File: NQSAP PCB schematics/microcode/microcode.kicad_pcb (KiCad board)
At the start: 2 copper layers, 102 x 96 mm, 58 parts, among them J1 Bus, J2 Bus, J5 Conn_02x08, J6 Conn_02x08, U1 28C256, U2 28C256, U3 28C256

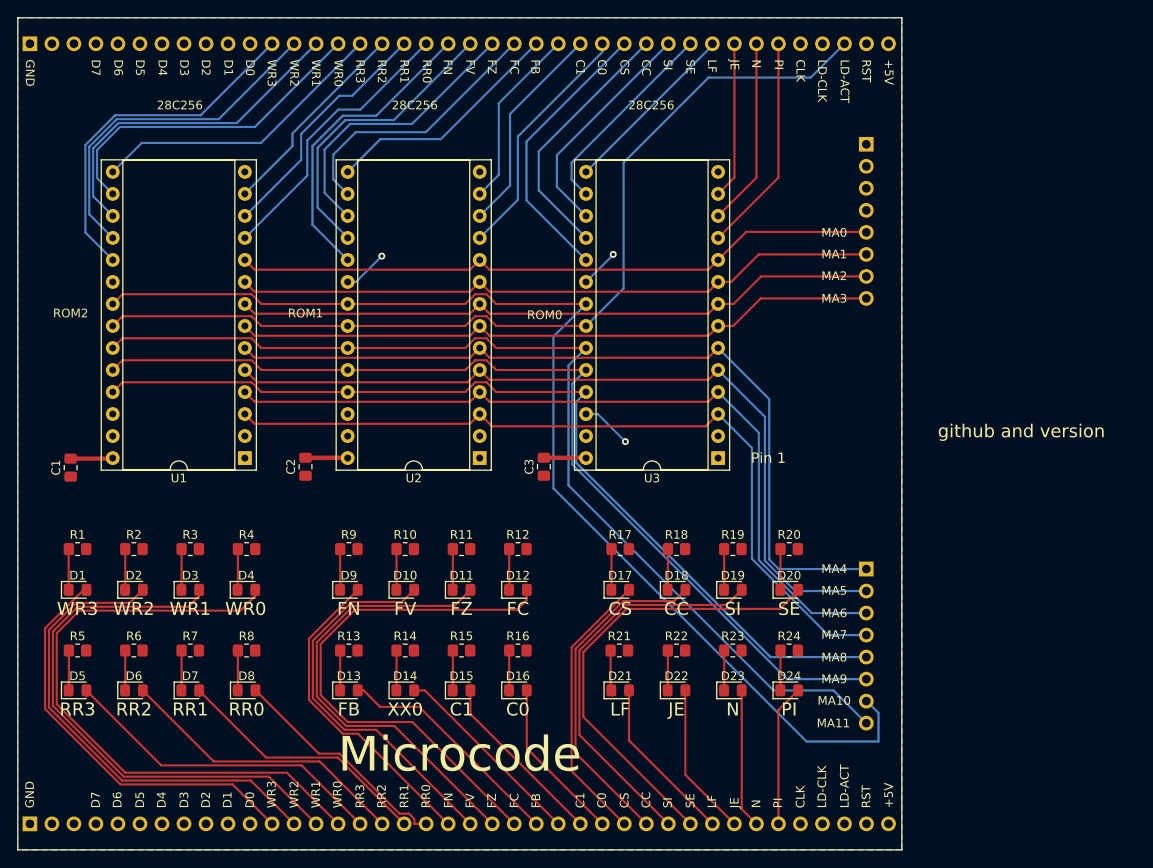
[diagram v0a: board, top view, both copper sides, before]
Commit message: Add Microcode and IR/RC modules.  Add clock circuit to Loader module.
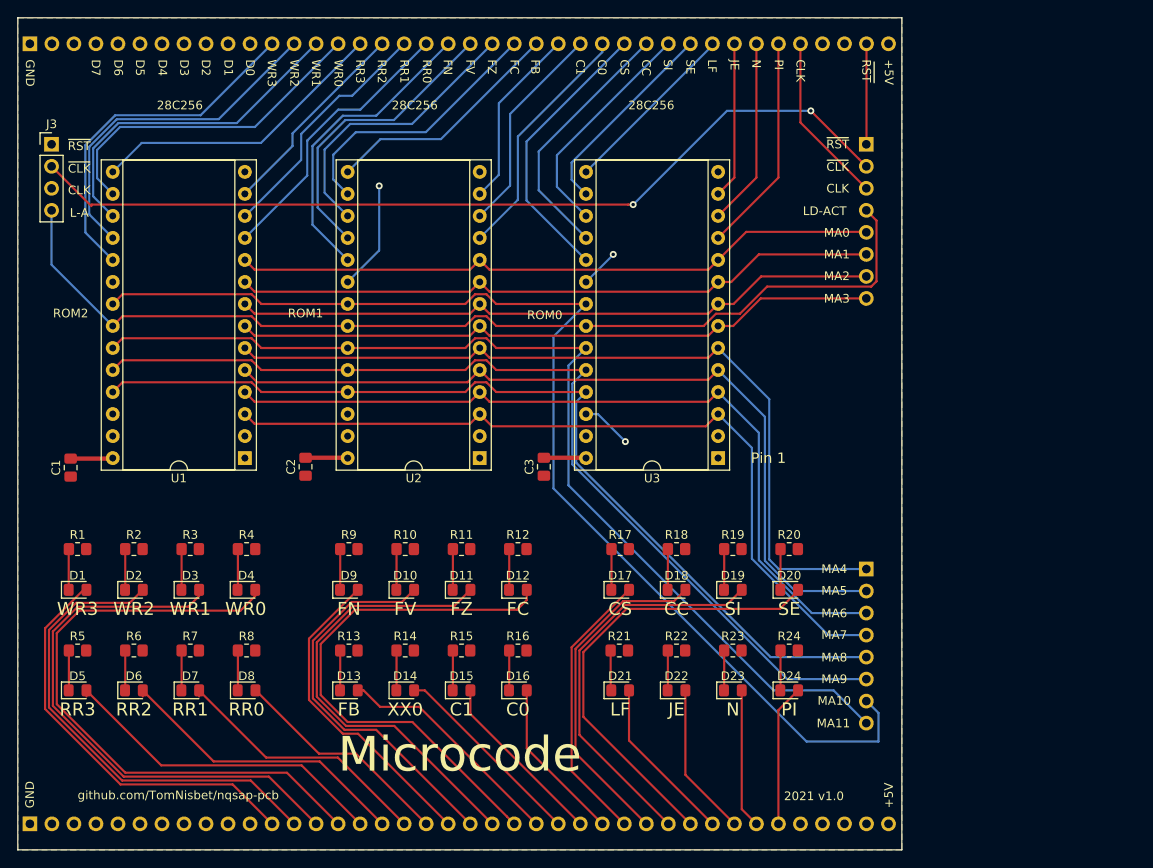
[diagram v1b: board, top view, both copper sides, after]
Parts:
- added J3: IC-LT, Connector_PinHeader_2.54mm:PinHeader_1x04_P2.54mm_Vertical, F.Cu at (88.9, 57.6)
- J5: value Conn_02x08 -> IC-RT
- J6: value Conn_02x08 -> IC-RB
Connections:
- J1 pad 36: Net-(J1-Pad36) -> CLK
- J1 pad 38: LD-ACT -> Net-(J1-Pad38)
- J1 pad 39: Net-(J1-Pad39) -> ~RST
- J5 pad 1: Net-(J5-Pad1) -> ~RST
- J5 pad 2: Net-(J5-Pad2) -> ~CLK
- J5 pad 3: Net-(J5-Pad3) -> CLK
- J5 pad 4: Net-(J5-Pad4) -> LD-ACT
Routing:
- net ~CLK: track 0.00 -> 103.3 mm, vias 0 -> 2
- net CLK: track 0.00 -> 19.8 mm
- net ~RST: track 0.00 -> 11.6 mm
- net LD-ACT: track 108.3 -> 117.0 mm
- net GND: track 15.5 -> 22.9 mm
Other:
- board text added: "2021 v1.0"
- board text added: "L-A"
- board text added: "github.com/TomNisbet/nqsap-pcb"
- board text added: "~CLK"
- board text added: "~RST"
- board text removed: "LD-CLK"
- board text removed: "github and version"

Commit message: Add RAM, update and add gerbers for new boards
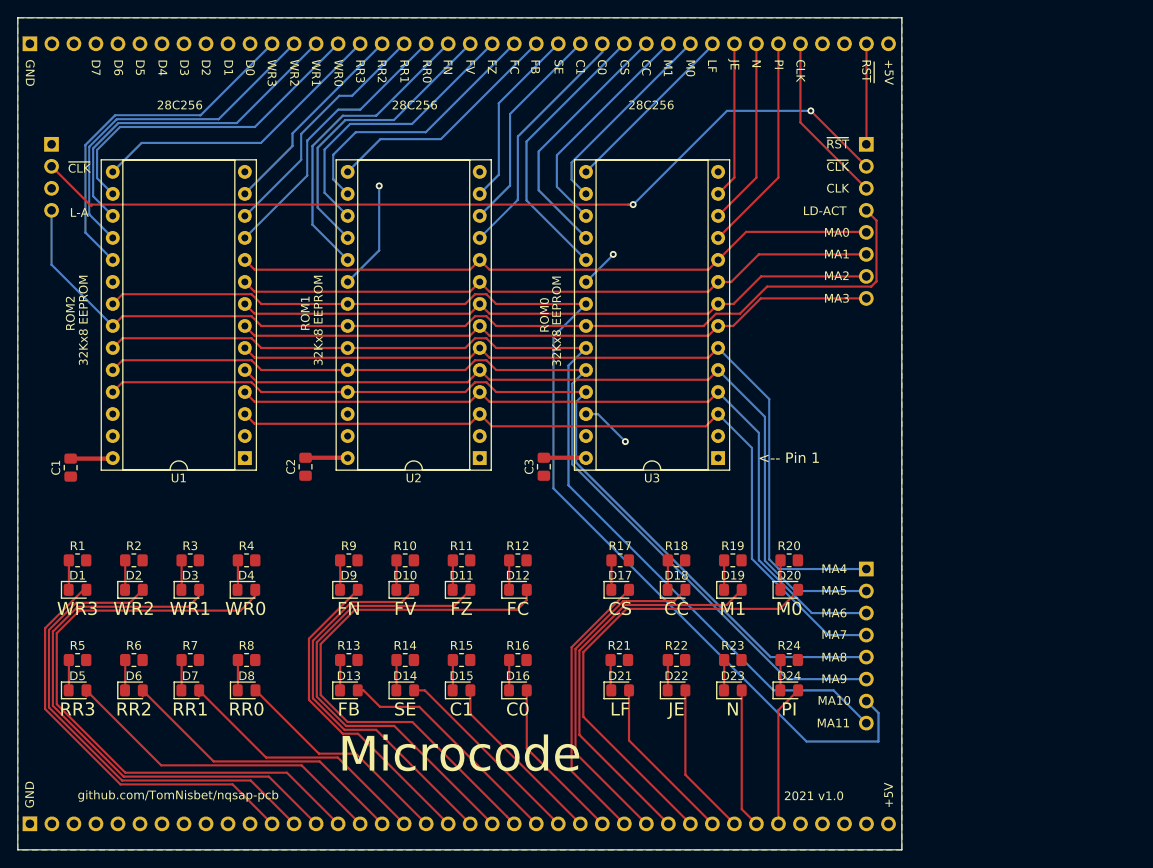
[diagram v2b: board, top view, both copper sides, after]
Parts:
- D14: value XX0 -> SE
- D19: value SI -> M1
- D20: value SE -> M0
- J3: moved to B.Cu
- moved R1 1.30 mm to (91.9, 105.6)
- moved R10 1.30 mm to (129.7, 105.6)
- moved R11 1.30 mm to (136.2, 105.6)
- moved R12 1.30 mm to (142.7, 105.6)
- moved R17 1.30 mm to (154.5, 105.6)
- moved R18 1.30 mm to (161.0, 105.6)
- moved R19 1.30 mm to (167.5, 105.6)
- moved R2 1.30 mm to (98.4, 105.6)
- moved R20 1.30 mm to (174.0, 105.6)
- moved R3 1.30 mm to (104.9, 105.6)
- moved R4 1.30 mm to (111.4, 105.6)
- moved R9 1.30 mm to (123.2, 105.6)
- moved R13 1.10 mm to (123.2, 117.1)
- moved R14 1.10 mm to (129.7, 117.1)
- moved R15 1.10 mm to (136.2, 117.1)
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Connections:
- net SI renamed M1
- D14 pad 2: XX0 -> SE
- D20 pad 2: SE -> M0
- J1 pad 25: XX0 -> SE
- J1 pad 31: SE -> M0
- J2 pad 25: XX0 -> SE
- J2 pad 31: SE -> M0
- J3 pad 1: ~RST -> Net-(J3-Pad1)
- J3 pad 3: CLK -> Net-(J3-Pad3)
- U2 pad 13: XX0 -> SE
- U3 pad 16: SE -> M0
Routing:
- net M0: track 0.00 -> 76.5 mm
- net XX0: track 44.1 -> 0.00 mm
- net SE: track 76.5 -> 44.1 mm
- net Net-(D9-Pad1): track 4.71 -> 3.41 mm
- net Net-(D4-Pad1): track 4.72 -> 3.42 mm
- net Net-(D3-Pad1): track 4.71 -> 3.41 mm
- net Net-(D20-Pad1): track 4.71 -> 3.41 mm
- net Net-(D2-Pad1): track 4.71 -> 3.41 mm
- net Net-(D19-Pad1): track 4.71 -> 3.41 mm
- net Net-(D18-Pad1): track 4.71 -> 3.41 mm
- net Net-(D17-Pad1): track 4.71 -> 3.41 mm
- net Net-(D12-Pad1): track 4.71 -> 3.41 mm
- net Net-(D11-Pad1): track 4.71 -> 3.41 mm
- net Net-(D10-Pad1): track 4.71 -> 3.41 mm
- net Net-(D1-Pad1): track 4.71 -> 3.45 mm
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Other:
- board text added: "<-- Pin 1"
- board text added: "M0"
- board text added: "M1"
- board text removed: "Pin 1"
- board text removed: "SI"
